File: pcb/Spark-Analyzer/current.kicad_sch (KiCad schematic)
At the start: 11 parts, among them IC3 CC6904SO-10A, Q1 DMP3017SFG-7, Q2 DTC143ECA-TP

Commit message: First app release and updated PCBA
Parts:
- removed TP5: TestPoint, TestPoint:TestPoint_Pad_D1.0mm, symbol Connector:TestPoint
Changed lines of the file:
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@@
   (junction (at 244.475 132.715) (diameter 0) (color 0 0 0 0)
   )
-  (junction (at 192.405 132.08) (diameter 0) (color 0 0 0 0)
-  )
   (junction (at 225.425 144.145) (diameter 0) (color 0 0 0 0)
   )
@@
     (stroke (width 0) (type default))
   )
-  (wire (pts (xy 192.405 132.08) (xy 204.47 132.08))
+  (wire (pts (xy 179.705 132.08) (xy 204.47 132.08))
     (stroke (width 0) (type default))
   )
@@
     (stroke (width 0) (type default))
   )
-  (wire (pts (xy 192.405 122.555) (xy 192.405 132.08))
-    (stroke (width 0) (type default))
-  )
   (wire (pts (xy 142.24 154.94) (xy 150.495 154.94))
     (stroke (width 0) (type default))
@@
   )
   (wire (pts (xy 225.425 144.145) (xy 225.425 145.415))
-    (stroke (width 0) (type default))
-  )
-  (wire (pts (xy 179.705 132.08) (xy 192.405 132.08))
     (stroke (width 0) (type default))
   )
@@
         )
       )
-    )
-  )
-  (symbol (lib_id "Connector:TestPoint") (at 192.405 122.555 0) (unit 1)
-    (in_bom yes) (on_board yes) (dnp no) (fields_autoplaced)
-    (property "Reference" "TP5" (at 193.802 118.6093 0)
-      (effects (font (size 1.27 1.27)) (justify left))
-    )
-    (property "Value" "TestPoint" (at 193.802 120.5303 0)
-      (effects (font (size 1.27 1.27)) (justify left))
-    )
-    (property "Footprint" "TestPoint:TestPoint_Pad_D1.0mm" (at 197.485 122.555 0)
-      (effects (font (size 1.27 1.27)) hide)
-    )
-    (property "Datasheet" "~" (at 197.485 122.555 0)
-      (effects (font (size 1.27 1.27)) hide)
-    )
-    (pin "1")
-    (instances
-      (project "Spark-Analyzer"
-        (path "/e63e39d7-6ac0-4ffd-8aa3-1841a4541b55/dc0e84e0-adcd-432b-9bb1-644eba2790b5"
-          (reference "TP5") (unit 1)
-        )
-        (path "/e63e39d7-6ac0-4ffd-8aa3-1841a4541b55/09249122-29b0-4dde-b4ca-260315792c2e"
-          (reference "TP7") (unit 1)
-        )
-      )

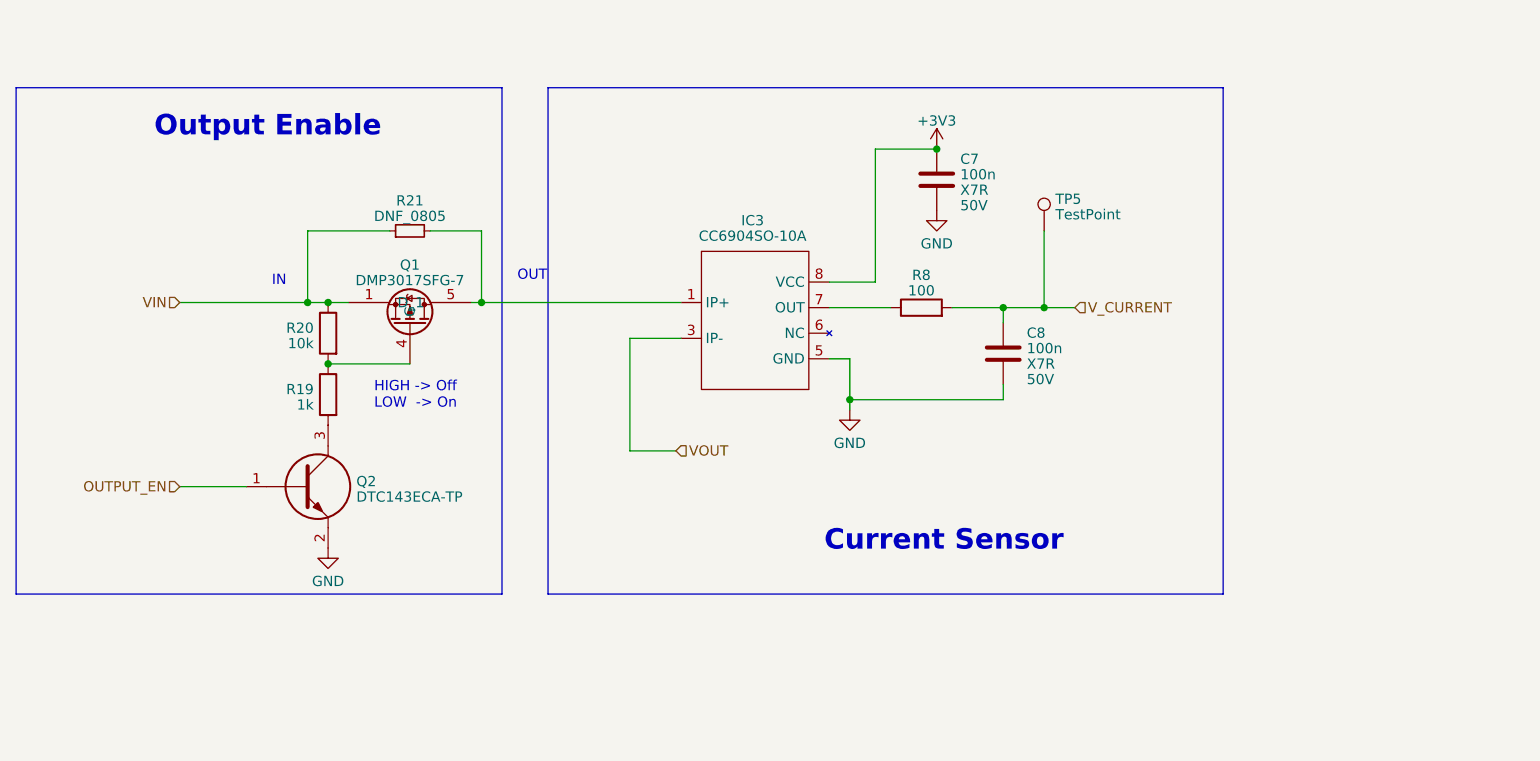
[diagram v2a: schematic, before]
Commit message: Switched current sensor
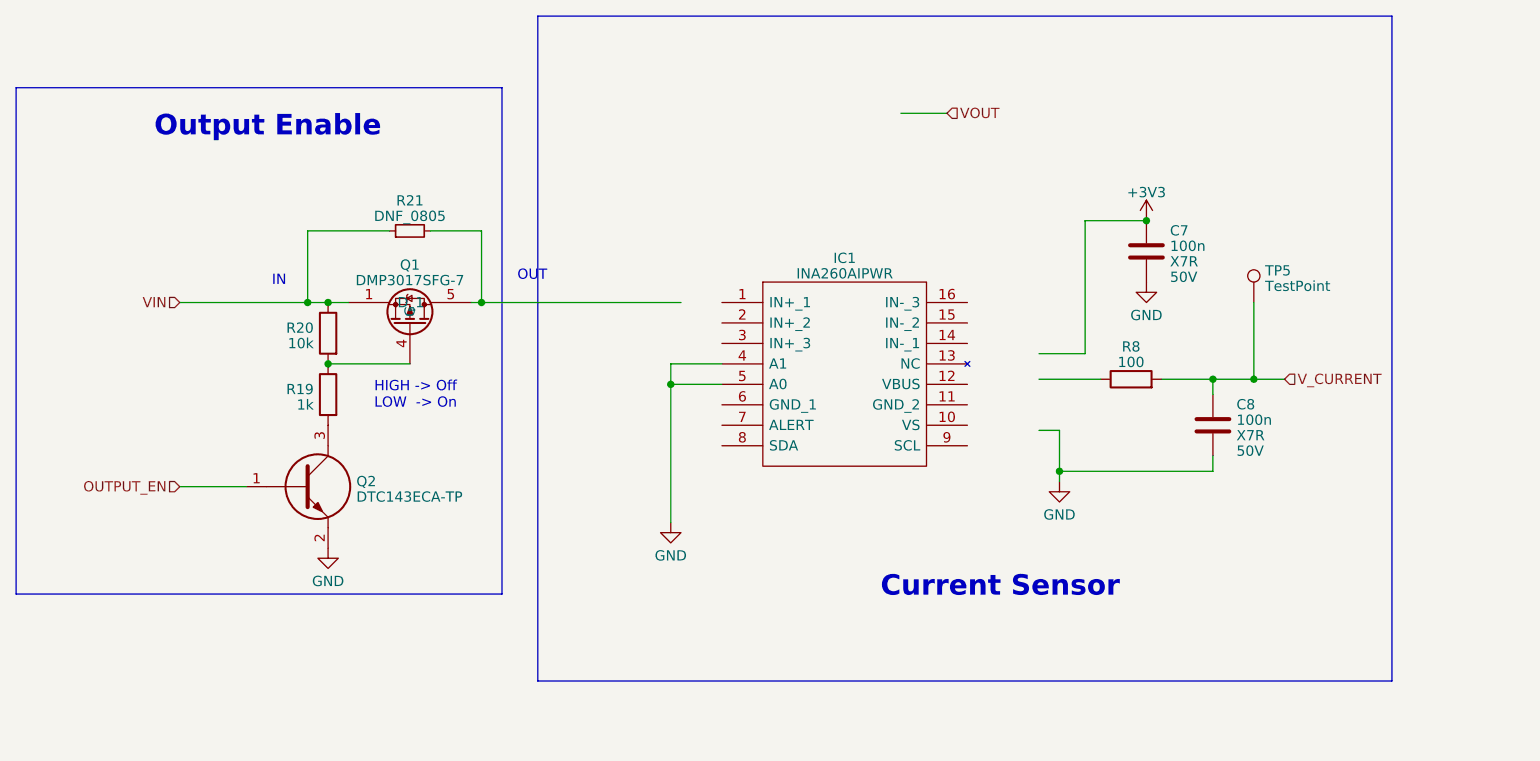
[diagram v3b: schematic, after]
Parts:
- removed IC3: CC6904SO-10A, Package_SO:SOP-8_3.9x4.9mm_P1.27mm, symbol Misc_JLC:CC6904SO-10A
- added IC1: INA260AIPWR, SOP65P640X120-16N, symbol Misc_JLC:INA260AIPWR
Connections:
- net GND: now also IC1.4 (A1), IC1.5 (A0)
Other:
- moved on the sheet: C7, C8, R8, TP5

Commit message: Wired sensor and changed connector
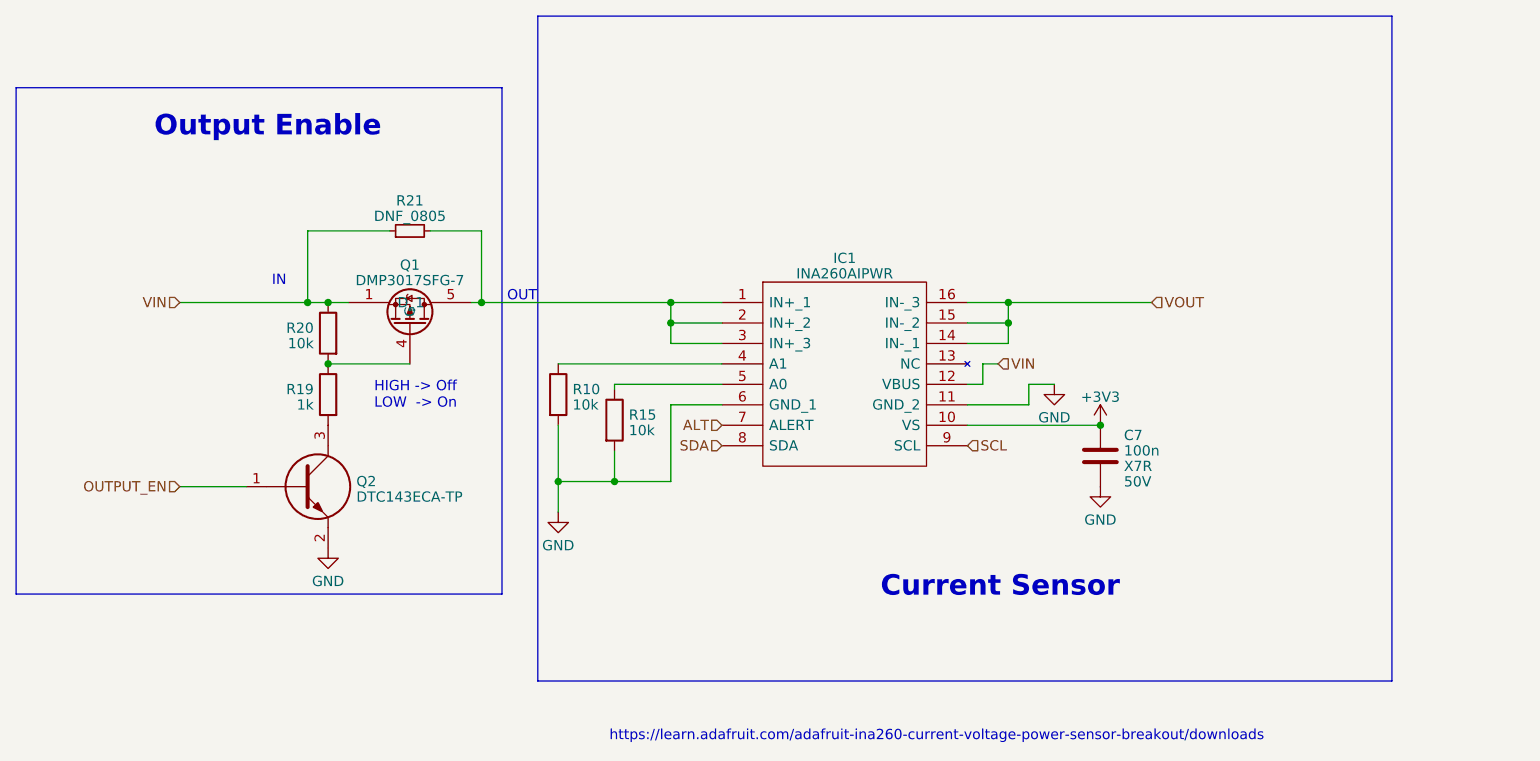
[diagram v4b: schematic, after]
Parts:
- removed C8: 100n, Capacitor_SMD:C_0402_1005Metric, symbol Capacitor_JLC:100n
- removed R8: 100, Resistor_SMD:R_0402_1005Metric, symbol Resistor_JLC:100
- removed TP5: TestPoint, TestPoint:TestPoint_Pad_D1.0mm, symbol Connector:TestPoint
- added R10, R15: 10k, Resistor_SMD:R_0402_1005Metric, symbol Resistor_JLC:10k
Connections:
- net +3V3: now also IC1.10 (VS)
- net GND: now also IC1.11 (GND_2), IC1.6 (GND_1), R10.2, R15.2; no longer IC1.4 (A1), IC1.5 (A0)
- net VIN: now also IC1.12 (VBUS)
- net VOUT: now also IC1.14 (IN-_1), IC1.15 (IN-_2), IC1.16 (IN-_3)
- net at Q1.5 (D_1), Q1.6, Q1.7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: now also IC1.1 (IN+_1), IC1.2 (IN+_2), IC1.3 (IN+_3)
- net ALT: now reaches IC1.7 (ALERT)
- net SDA: now reaches IC1.8 (SDA)
- net SCL: now reaches IC1.9 (SCL)
- new net: IC1.4 (A1), R10.1
- new net: IC1.5 (A0), R15.1
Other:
- note added: "https://learn.adafruit.com/adafruit-ina260-current-voltage-power-sensor-breakout/downloads"
- moved on the sheet: C7

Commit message: To be reviewed
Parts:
- renumbered Q2 to Q1, Q1 to Q2, R20 to R19, R19 to R20
